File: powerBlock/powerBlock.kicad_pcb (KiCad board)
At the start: 2 copper layers, 3 parts, among them U1 STM32F030C8Tx, U2 74HC164, U3 74HC164

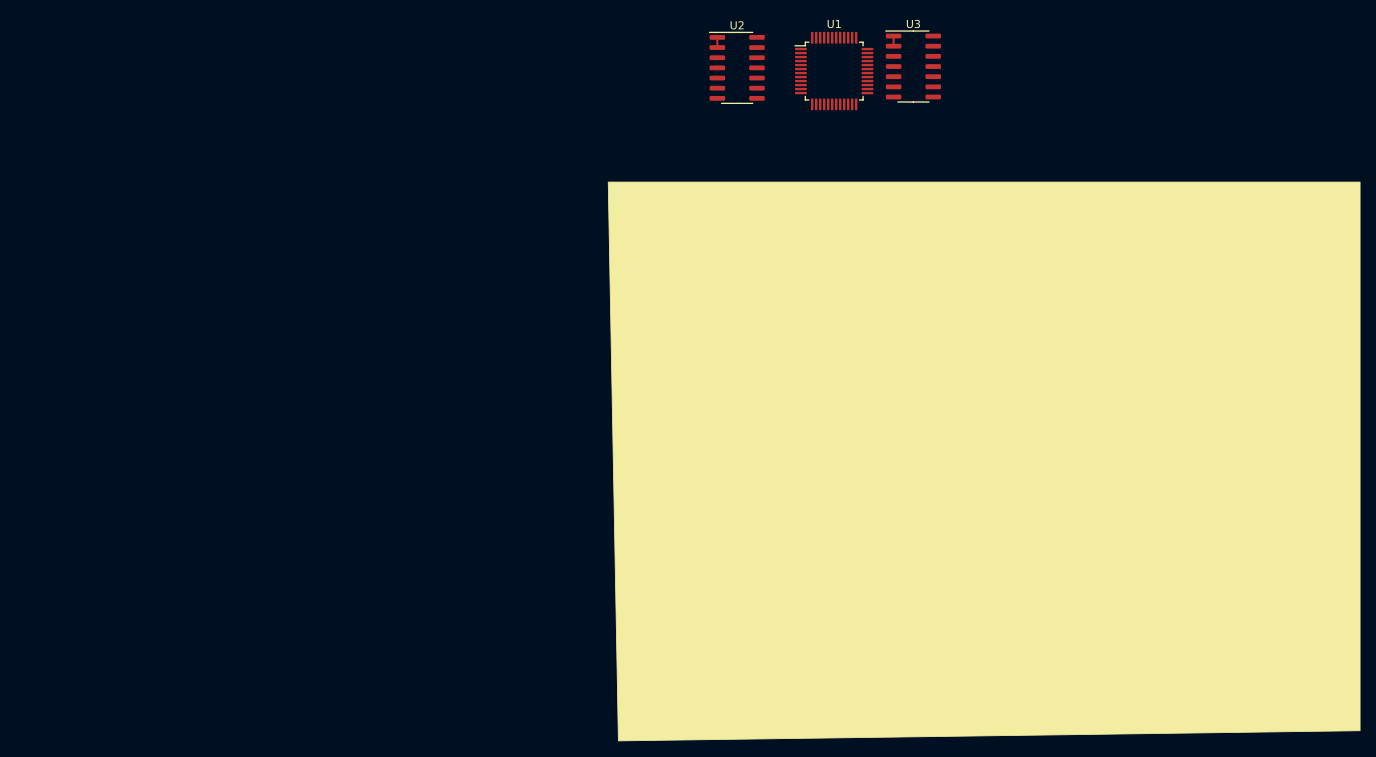
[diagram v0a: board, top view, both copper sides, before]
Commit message: Добавил индикаторную панель. Подключил диод
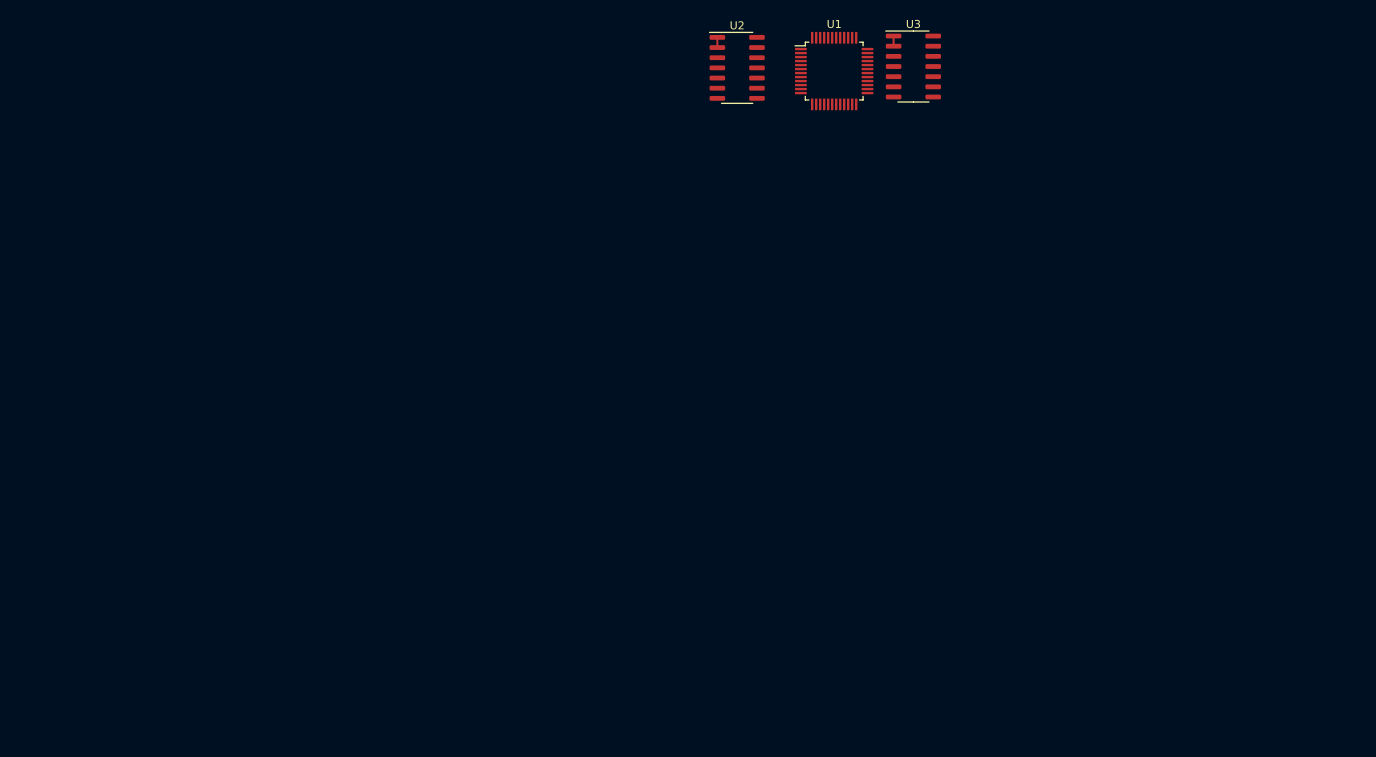
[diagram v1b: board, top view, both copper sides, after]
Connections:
- U1 pad 28: Net-(U1-Pad28) -> /SPI2MOSI
- U2 pad 1: Net-(U2-Pad1) -> /SPI2MOSI
- U2 pad 2: Net-(U2-Pad1) -> /SPI2MOSI
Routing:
- net Net-(U2-Pad1): track 1.27 -> 0.00 mm
- net /SPI2MOSI: track 0.00 -> 1.27 mm

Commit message: Немного допилил схему. Немного оттрассировал
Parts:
- added C1: 10uF, Capacitor_SMD:C_0603_1608Metric, F.Cu at (111.1, 58.7)
- added C10: 10uF, Capacitor_SMD:C_0603_1608Metric, F.Cu at (124.3, 53.2)
- added C11: 10uF, Capacitor_SMD:C_0603_1608Metric, F.Cu at (121.3, 53.2)
- added C2: 100nF, Capacitor_SMD:C_0603_1608Metric, F.Cu at (96.3, 59.5)
- added C3: 100nF, Capacitor_SMD:C_0603_1608Metric, F.Cu at (93.3, 59.5)
- added C4: 1uF, Capacitor_SMD:C_0603_1608Metric, F.Cu at (94.5, 74.8)
- added C5: 1uF, Capacitor_SMD:C_0603_1608Metric, F.Cu at (103.0, 85.3)
- added C6: 1uF, Capacitor_SMD:C_0603_1608Metric, F.Cu at (108.5, 76.3)
- added C7: 1uF, Capacitor_SMD:C_0603_1608Metric, F.Cu at (123.0, 76.3)
- added C8: 1uF, Capacitor_SMD:C_0603_1608Metric, F.Cu at (124.5, 87.2)
- added C9: 1uF, Capacitor_SMD:C_0603_1608Metric, F.Cu at (109.6, 66.6)
- added D1: LED, LED_THT:LED_Rectangular_W3.9mm_H1.8mm, F.Cu at (113.0, 98.5)
- added D10: DO-214AC, Diode_SMD:D_SMA, F.Cu at (96.0, 87.5)
- added D11: DO-214AC, Diode_SMD:D_SMA, F.Cu at (101.5, 78.5)
- added D12: DO-214AC, Diode_SMD:D_SMA, F.Cu at (116.0, 78.5)
- added D13: DO-214AC, Diode_SMD:D_SMA, F.Cu at (118.0, 89.5)
- added D2: LED, LED_THT:LED_Rectangular_W3.9mm_H1.8mm, F.Cu at (107.0, 98.5)
- added D3: LED, LED_THT:LED_Rectangular_W3.9mm_H1.8mm, F.Cu at (101.0, 98.5)
- added D4: LED, LED_THT:LED_Rectangular_W3.9mm_H1.8mm, F.Cu at (95.0, 98.5)
- added D5: LED, LED_THT:LED_Rectangular_W3.9mm_H1.8mm, F.Cu at (89.0, 98.5)
- added D7: LED, LED_THT:LED_Rectangular_W3.9mm_H1.8mm, F.Cu at (70.0, 98.5)
- added D8: LED, LED_THT:LED_Rectangular_W3.9mm_H1.8mm, F.Cu at (63.0, 98.5)
- added D9: DO-214AC, Diode_SMD:D_SMA, F.Cu at (88.5, 77.0)
- added J1: Conn_01x04, Connector_PinHeader_2.54mm:PinHeader_1x04_P2.54mm_Vertical, F.Cu at (116.5, 60.0)
- added J2: Conn_01x10, Connector_PinHeader_2.54mm:PinHeader_1x10_P2.54mm_Horizontal, F.Cu at (39.0, 81.5)
- added J3: 282844-2, TerminalBlock_MetzConnect:TerminalBlock_MetzConnect_Type175_RT02702HBLC_1x02_P7.50mm_Horizontal, F.Cu at (134.0, 50.0)
- added LS1: Speaker_Crystal, OptoDevice:R_LDR_10x8.5mm_P7.6mm_Vertical, F.Cu at (97.0, 53.1)
- added Q1: BC857BMTF, Package_TO_SOT_SMD:SOT-23, F.Cu at (65.5, 56.5)
- added Q2: BC857BMTF, Package_TO_SOT_SMD:SOT-23, F.Cu at (65.5, 51.0)
- added Q3: BC857BMTF, Package_TO_SOT_SMD:SOT-23, F.Cu at (65.5, 45.5)
- added Q4: BC857BMTF, Package_TO_SOT_SMD:SOT-23, F.Cu at (114.5, 51.5)
- added R1: 18kOhm, Resistor_SMD:R_0603_1608Metric, F.Cu at (55.3, 70.0)
- added R10: 270, Resistor_SMD:R_0603_1608Metric, F.Cu at (109.5, 96.8)
- added R11: 270, Resistor_SMD:R_0603_1608Metric, F.Cu at (103.5, 96.8)
- added R12: 270, Resistor_SMD:R_0603_1608Metric, F.Cu at (97.5, 96.8)
- added R13: 270, Resistor_SMD:R_0603_1608Metric, F.Cu at (91.5, 96.8)
- added R14: 270, Resistor_SMD:R_0603_1608Metric, F.Cu at (73.5, 96.8)
- added R15: 270, Resistor_SMD:R_0603_1608Metric, F.Cu at (65.5, 96.7)
- added R16: 4.3kOhm, Resistor_SMD:R_0603_1608Metric, F.Cu at (86.0, 75.2)
- added R17: 4.3kOhm, Resistor_SMD:R_0603_1608Metric, F.Cu at (92.0, 85.8)
- added R18: 470 Ohm, Resistor_SMD:R_0603_1608Metric, F.Cu at (100.0, 85.3)
- added R19: 4.3kOhm, Resistor_SMD:R_0603_1608Metric, F.Cu at (97.5, 76.5)
- added R2: 18kOhm, Resistor_SMD:R_0603_1608Metric, F.Cu at (55.3, 60.0)
- added R20: 470 Ohm, Resistor_SMD:R_0603_1608Metric, F.Cu at (105.5, 76.3)
- added R21: 4.3kOhm, Resistor_SMD:R_0603_1608Metric, F.Cu at (112.0, 76.3)
- added R22: 470 Ohm, Resistor_SMD:R_0603_1608Metric, F.Cu at (120.0, 76.3)
- added R23: 4.3kOhm, Resistor_SMD:R_0603_1608Metric, F.Cu at (113.5, 87.8)
- added R24: 470 Ohm, Resistor_SMD:R_0603_1608Metric, F.Cu at (121.5, 87.5)
- added R25: 470Ohm, Resistor_SMD:R_0603_1608Metric, F.Cu at (91.5, 74.8)
- added R26: 10kOhm, Resistor_SMD:R_0603_1608Metric, F.Cu at (89.0, 47.2)
- added R27: 330 Ohm, Resistor_SMD:R_0603_1608Metric, F.Cu at (111.5, 52.3)
- added R3: 18kOhm, Resistor_SMD:R_0603_1608Metric, F.Cu at (71.2, 65.0)
- added R4: 18kOhm, Resistor_SMD:R_0603_1608Metric, F.Cu at (71.2, 70.5)
- added R5: 18kOhm, Resistor_SMD:R_0603_1608Metric, F.Cu at (71.8, 72.5)
- added R6: 18kOhm, Resistor_SMD:R_0603_1608Metric, F.Cu at (55.2, 67.5)
- added R7: 18kOhm, Resistor_SMD:R_0603_1608Metric, F.Cu at (71.3, 62.0)
- added R8: 18kOhm, Resistor_SMD:R_0603_1608Metric, F.Cu at (66.8, 66.5)
- added R9: 270, Resistor_SMD:R_0603_1608Metric, F.Cu at (115.5, 96.8)
- added RV1: TC33X-2-502E, Potentiometer_SMD:Potentiometer_Bourns_TC33X_Vertical, F.Cu at (107.0, 46.0)
- added SW1: SW_MEC_5G, Button_Switch_SMD:SW_SPST_PTS645, F.Cu at (84.8, 51.5)
- added U4: BA56-12SRWA, Display_7Segment:CA56-12SEKWA, F.Cu at (75.2, 72.7)
- added U5: LD1086DT50TR, Package_TO_SOT_SMD:TO-252-2, F.Cu at (121.5, 43.3)
- added U6: AP2127K-3.3, Package_TO_SOT_SMD:SOT-23-5, F.Cu at (106.8, 57.0)
- moved U3 65.9 mm to (83.0, 62.5)
- moved U2 46.5 mm to (130.5, 76.5), turned to 270 degrees
- moved U1 45.6 mm to (101.5, 66.5)
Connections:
- U1 pad 1: Net-(U1-Pad1) -> +3V3
- U1 pad 13: Net-(U1-Pad13) -> /ADC3
- U1 pad 14: Net-(U1-Pad14) -> /ADC4
- U1 pad 15: Net-(U1-Pad15) -> /ADC5
- U1 pad 16: Net-(U1-Pad16) -> /ADC6
- U1 pad 17: Net-(U1-Pad17) -> /ADC7
- U1 pad 23: Net-(U1-Pad23) -> GND
- U1 pad 24: Net-(U1-Pad24) -> +3V3
- U1 pad 26: Net-(U1-Pad26) -> /SPI2CLK
- U1 pad 34: Net-(U1-Pad34) -> /SWDIO
- U1 pad 37: Net-(U1-Pad37) -> /SWCLK
- U1 pad 39: Net-(U1-Pad39) -> /SPI1CLK
- U1 pad 40: Net-(U1-Pad40) -> /GPIOB4
- U1 pad 41: Net-(U1-Pad41) -> /SPI1MOSI
- U1 pad 42: Net-(U1-Pad42) -> /GPIOB6
- U1 pad 43: Net-(U1-Pad43) -> /GPIOB7
- U1 pad 45: Net-(U1-Pad45) -> /GPIOB8
- U1 pad 47: Net-(U1-Pad47) -> GND
- U1 pad 48: Net-(U1-Pad48) -> +3V3
- U1 pad 8: Net-(U1-Pad8) -> GND
- U1 pad 9: Net-(U1-Pad9) -> +3V3
- U2 pad 14: Net-(U2-Pad14) -> +5V
- U2 pad 7: Net-(U2-Pad7) -> GND
- U2 pad 8: Net-(U2-Pad8) -> /SPI2CLK
- U2 pad 9: Net-(U2-Pad9) -> +5V
- U3 pad 1: Net-(U3-Pad1) -> /SPI1MOSI
- U3 pad 14: Net-(U3-Pad14) -> +5V
- U3 pad 2: Net-(U3-Pad1) -> /SPI1MOSI
- U3 pad 7: Net-(U3-Pad7) -> GND
- U3 pad 8: Net-(U3-Pad8) -> /SPI1CLK
- U3 pad 9: Net-(U3-Pad9) -> +5V
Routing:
- net Net-(R10-Pad1): track 0.00 -> 60.9 mm, vias 0 -> 2
- net Net-(R9-Pad1): track 0.00 -> 44.7 mm, vias 0 -> 2
- net +3V3: track 0.00 -> 40.6 mm
- net /SPI2MOSI: track 1.27 -> 33.0 mm
- net /SPI2CLK: track 0.00 -> 26.5 mm
- net +5VA: track 0.00 -> 20.8 mm
- net /SWCLK: track 0.00 -> 18.3 mm, vias 0 -> 1
- net /SWDIO: track 0.00 -> 16.0 mm
- net /ADC5: track 0.00 -> 11.7 mm
- net Net-(C9-Pad1): track 0.00 -> 3.99 mm
- net Net-(D7-Pad2): track 0.00 -> 3.52 mm
- net Net-(R12-Pad1): track 0.00 -> 2.84 mm, vias 0 -> 1
- net Net-(D8-Pad2): track 0.00 -> 2.53 mm
- net Net-(D5-Pad2): track 0.00 -> 2.52 mm
- net Net-(D4-Pad2): track 0.00 -> 2.52 mm
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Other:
- board outline added: 105 x 80 mm
